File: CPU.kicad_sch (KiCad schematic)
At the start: 14 parts, among them J8 SWD, U4 STM32F405RGTx, Y1 8MHz

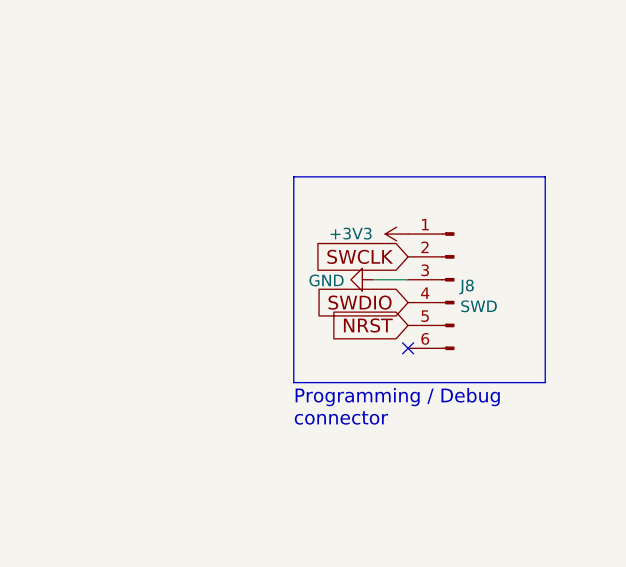
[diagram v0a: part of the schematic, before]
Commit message: HSWR V4.1: - added opamp for better voltage measurement
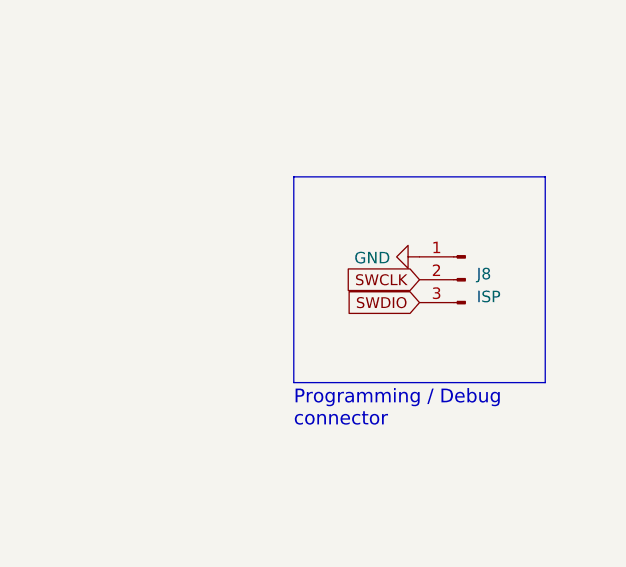
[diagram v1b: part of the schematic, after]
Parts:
- removed J8: SWD, Connector_PinHeader_2.54mm:PinHeader_2x03_P2.54mm_Vertical, symbol HSWR-rescue:Conn_01x06_Male-Connector
- added J8: ISP, Connector_PinHeader_2.54mm:PinHeader_1x03_P2.54mm_Vertical, symbol Connector:Conn_01x03_Pin
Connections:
- net GND: now also J8.1 (Pin_1)
- net SWCLK: now also J8.2 (Pin_2)
- net SWDIO: now also J8.3 (Pin_3)
- no-connect marks 19 -> 18
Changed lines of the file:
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@@
   )
   (no_connect (at 127 106.68))
-  (no_connect (at 247.65 86.36))
   (no_connect (at 162.56 101.6))
   (no_connect (at 127 129.54))
@@
     (stroke (width 0) (type default))
   )
-  (wire (pts (xy 247.65 78.74) (xy 243.84 78.74))
-    (stroke (width 0) (type default))
-  )
   (polyline (pts (xy 234.95 67.31) (xy 234.95 90.17))
     (stroke (width 0) (type default))
@@
     )
   )
-  (global_label "SWDIO" (shape input) (at 247.65 81.28 180)
-    (effects (font (size 1.524 1.524)) (justify right))
-    (property "Intersheetrefs" "${INTERSHEET_REFS}" (at 247.65 81.28 0)
+  (global_label "SWDIO" (shape input) (at 248.92 81.28 180)
+    (effects (font (size 1.2 1.2)) (justify right))
+    (property "Intersheetrefs" "${INTERSHEET_REFS}" (at 248.92 81.28 0)
       (effects (font (size 1.27 1.27)) hide)
     )
@@
     )
   )
-  (global_label "NRST" (shape input) (at 247.65 83.82 180)
-    (effects (font (size 1.524 1.524)) (justify right))
-    (property "Intersheetrefs" "${INTERSHEET_REFS}" (at 247.65 83.82 0)
-      (effects (font (size 1.27 1.27)) hide)
-    )
-  )
-  (global_label "SWCLK" (shape input) (at 247.65 76.2 180)
-    (effects (font (size 1.524 1.524)) (justify right))
-    (property "Intersheetrefs" "${INTERSHEET_REFS}" (at 247.65 76.2 0)
+  (global_label "SWCLK" (shape input) (at 248.92 78.74 180)
+    (effects (font (size 1.2 1.2)) (justify right))
+    (property "Intersheetrefs" "${INTERSHEET_REFS}" (at 248.92 78.74 0)
       (effects (font (size 1.27 1.27)) hide)
     )
@@
     (effects (font (size 1.27 1.27)) (justify left))
   )
-  (symbol (lib_id "power:+3V3") (at 247.65 73.66 90) (unit 1)
-    (in_bom yes) (on_board yes) (dnp no)
-    (property "Reference" "#PWR082" (at 251.46 73.66 0)
-      (effects (font (size 1.27 1.27)) hide)
-    )
-    (property "Value" "+3V3" (at 241.3 73.66 90)
-      (effects (font (size 1.27 1.27)))
-    )
-    (property "Footprint" "" (at 247.65 73.66 0)
-      (effects (font (size 1.27 1.27)))
-    )
-    (property "Datasheet" "" (at 247.65 73.66 0)
-      (effects (font (size 1.27 1.27)))
-    )
-    (pin "1")
-    (instances
-      (project "HSWR"
-        (path "/51094070-255e-40e7-bed5-d199e288e5dd/00000000-0000-0000-0000-00005899e230"
-          (reference "#PWR082") (unit 1)
-        )
-      )
-    )
-  )
   (symbol (lib_id "power:+3V3") (at 231.14 24.13 0) (unit 1)
     (in_bom yes) (on_board yes) (dnp no)
@@
     )
   )
-  (symbol (lib_id "HSWR-rescue:Conn_01x06_Male-Connector") (at 252.73 78.74 0) (mirror y) (unit 1)
+  (symbol (lib_id "power:GND") (at 248.92 76.2 270) (unit 1)
     (in_bom yes) (on_board yes) (dnp no)
-    (property "Reference" "J8" (at 253.4412 79.4258 0)
-      (effects (font (size 1.27 1.27)) (justify right))
-    )
-    (property "Value" "SWD" (at 253.4412 81.7372 0)
-      (effects (font (size 1.27 1.27)) (justify right))
-    )
-    (property "Footprint" "Connector_PinHeader_2.54mm:PinHeader_2x03_P2.54mm_Vertical" (at 252.73 78.74 0)
-      (effects (font (size 1.27 1.27)) hide)
-    )
-    (property "Datasheet" "~" (at 252.73 78.74 0)
+    (property "Reference" "#PWR081" (at 242.57 76.2 0)
       (effects (font (size 1.27 1.27)) hide)
     )
-    (pin "1")
-    (pin "2")
-    (pin "3")
-    (pin "4")
-    (pin "5")
-    (pin "6")
-    (instances
-      (project "HSWR"
-        (path "/51094070-255e-40e7-bed5-d199e288e5dd/00000000-0000-0000-0000-00005899e230"
-          (reference "J8") (unit 1)
-        )
-      )
-    )
-  )
-  (symbol (lib_id "power:GND") (at 243.84 78.74 270) (unit 1)
-    (in_bom yes) (on_board yes) (dnp no)
-    (property "Reference" "#PWR081" (at 237.49 78.74 0)
-      (effects (font (size 1.27 1.27)) hide)
-    )
-    (property "Value" "GND" (at 240.5888 78.867 90)
+    (property "Value" "GND" (at 245.6688 76.327 90)
       (effects (font (size 1.27 1.27)) (justify right))
     )
-    (property "Footprint" "" (at 243.84 78.74 0)
+    (property "Footprint" "" (at 248.92 76.2 0)
       (effects (font (size 1.27 1.27)) hide)
     )
-    (property "Datasheet" "" (at 243.84 78.74 0)
+    (property "Datasheet" "" (at 248.92 76.2 0)
       (effects (font (size 1.27 1.27)) hide)
     )
@@
         )
       )
+    )
+  )
+  (symbol (lib_id "Connector:Conn_01x03_Pin") (at 254 78.74 0) (mirror y) (unit 1)
+    (in_bom yes) (on_board yes) (dnp no) (fields_autoplaced)
+    (property "Reference" "J8" (at 255.27 78.105 0)
+      (effects (font (size 1.27 1.27)) (justify right))
+    )
+    (property "Value" "ISP" (at 255.27 80.645 0)
+      (effects (font (size 1.27 1.27)) (justify right))
+    )
+    (property "Footprint" "Connector_PinHeader_2.54mm:PinHeader_1x03_P2.54mm_Vertical" (at 254 78.74 0)
+      (effects (font (size 1.27 1.27)) hide)
+    )
+    (property "Datasheet" "~" (at 254 78.74 0)
+      (effects (font (size 1.27 1.27)) hide)
+    )
+    (pin "1")
+    (pin "2")
+    (pin "3")
+    (instances
+      (project "HSWR"
+        (path "/51094070-255e-40e7-bed5-d199e288e5dd/00000000-0000-0000-0000-00005899e230"
+          (reference "J8") (unit 1)
+        )
+      )
